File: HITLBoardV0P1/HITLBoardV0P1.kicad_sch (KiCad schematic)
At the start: 0 parts

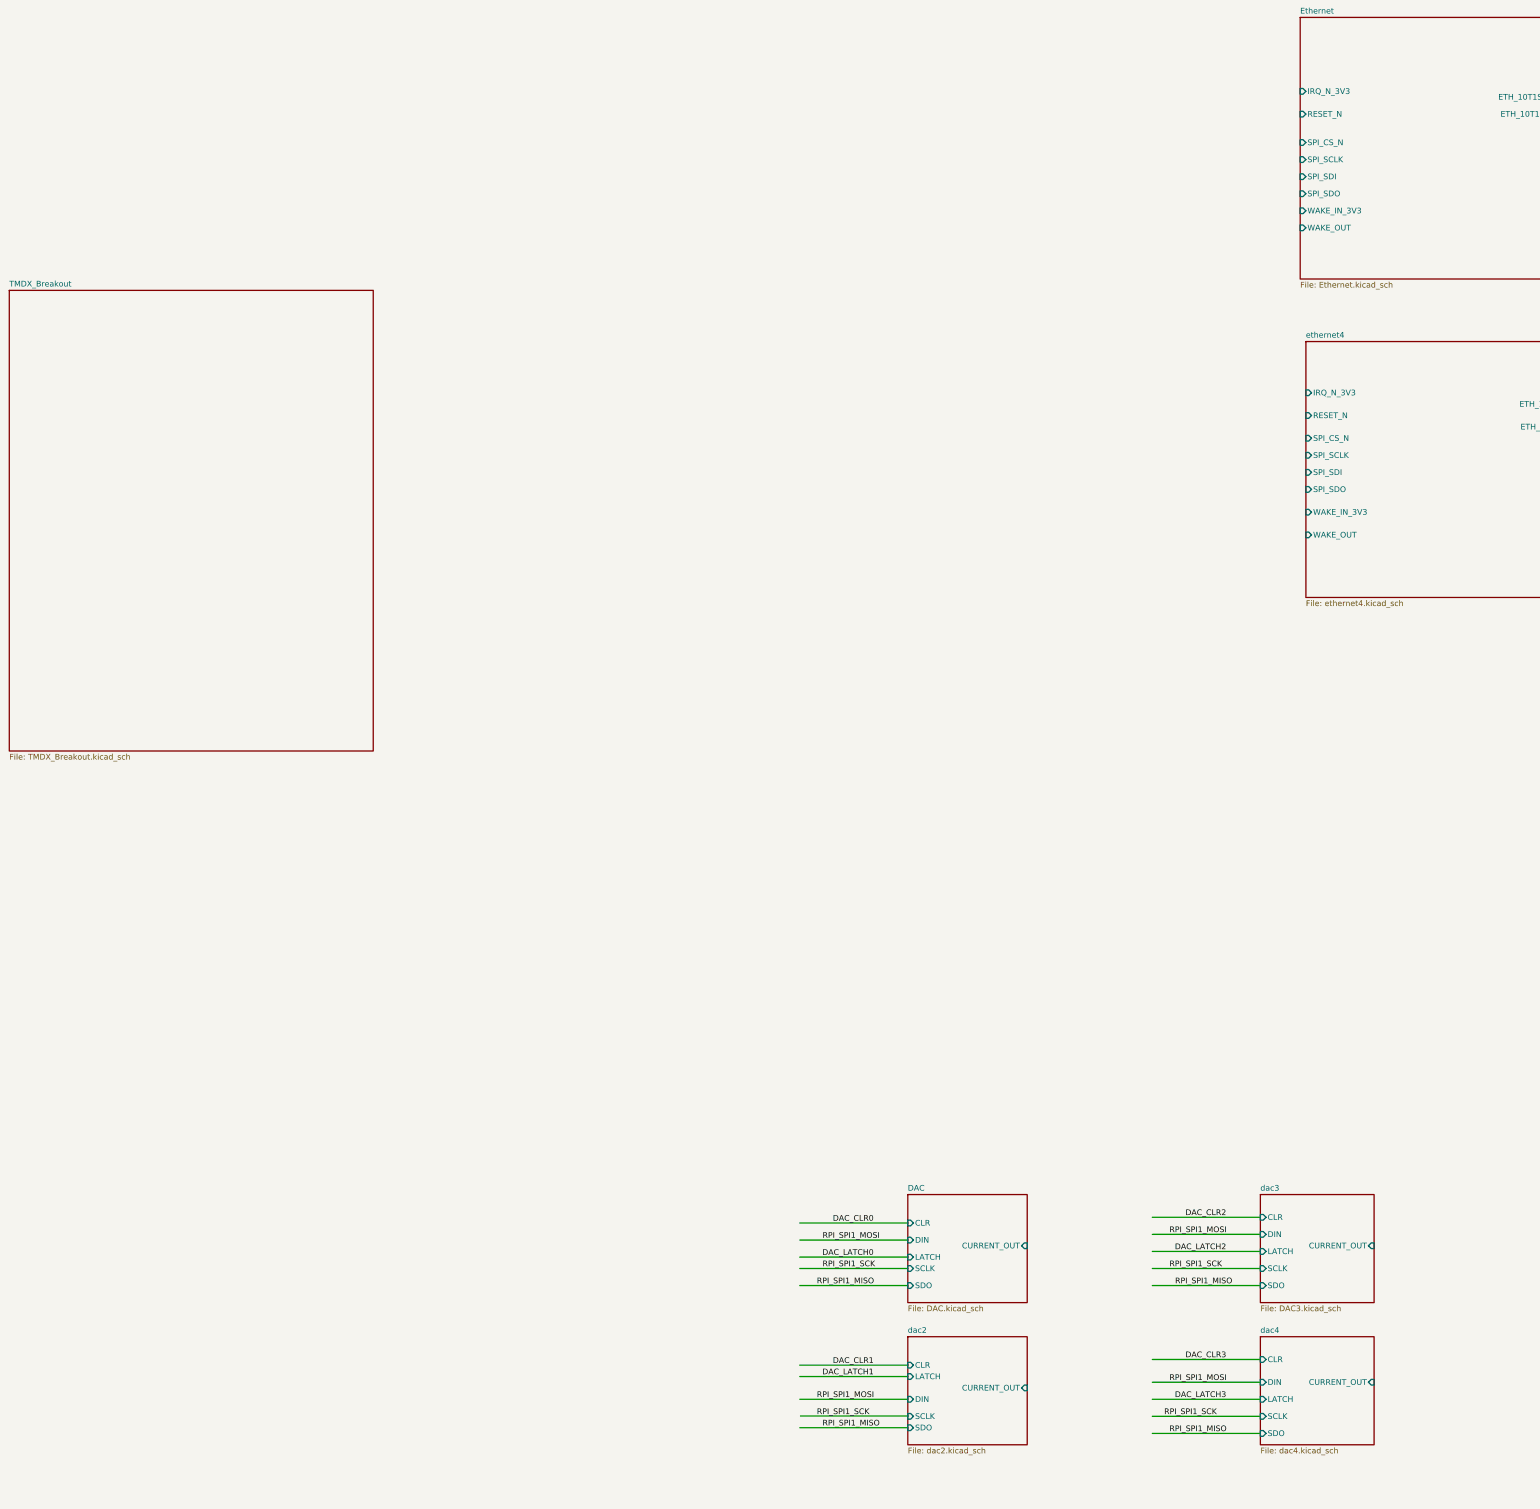
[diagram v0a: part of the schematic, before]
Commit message: update to board with spi buses assigned
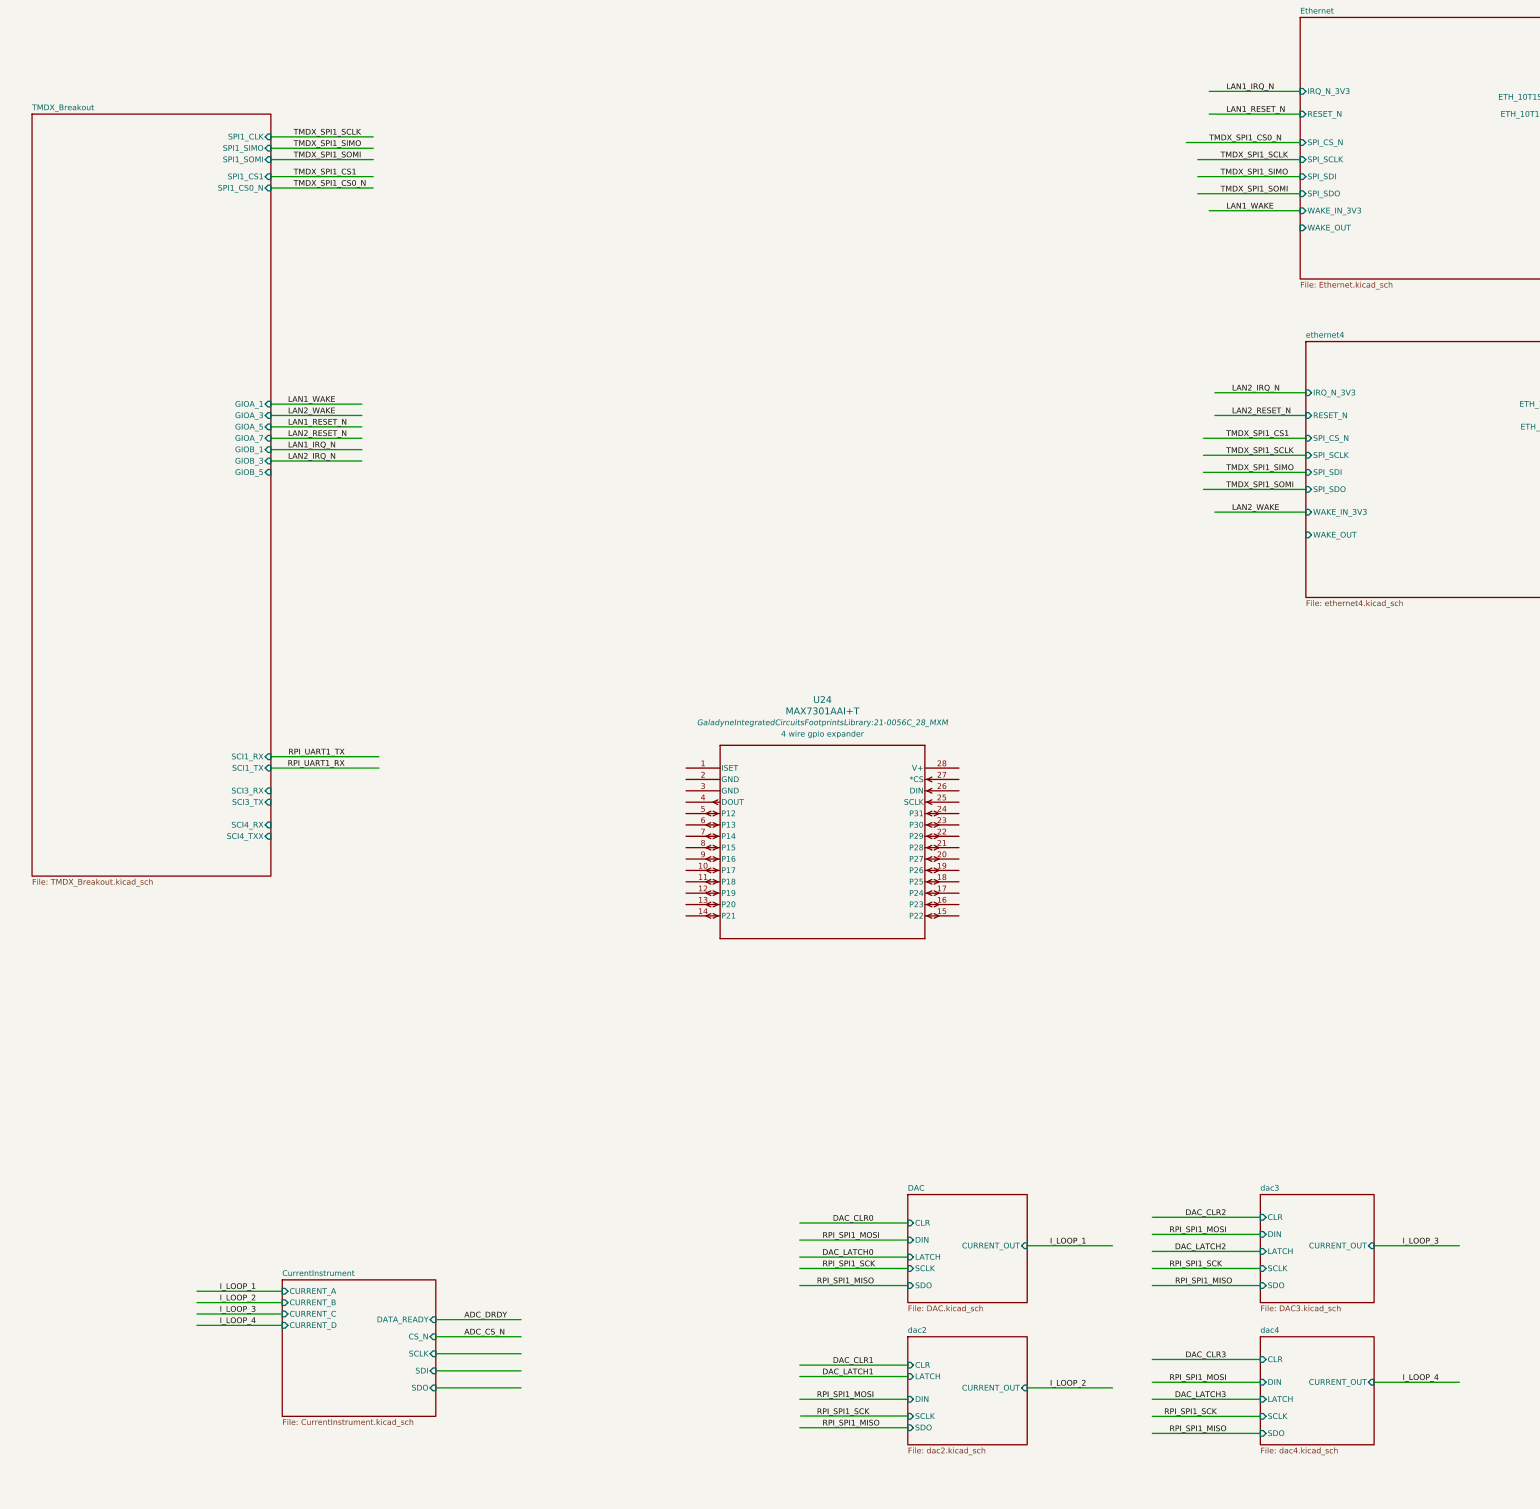
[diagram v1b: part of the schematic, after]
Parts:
- added U24: MAX7301AAI+T, GaladyneIntegratedCircuitsFootprintsLibrary:21-0056C_28_MXM, symbol GaladyneIntegratedCircuitsLibrary:MAX7301AAI+T
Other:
- added sheet CurrentInstrument (CurrentInstrument.kicad_sch)
- sheet TMDX_Breakout ports: added GIOA_1, GIOA_3, GIOA_5, GIOA_7, GIOB_1, GIOB_3, GIOB_5, SCI1_RX, SCI1_TX, SCI3_RX, SCI3_TX, SCI4_RX, SCI4_TXX, SPI1_CLK, SPI1_CS0_N, SPI1_CS1, SPI1_SIMO, SPI1_SOMI; removed none

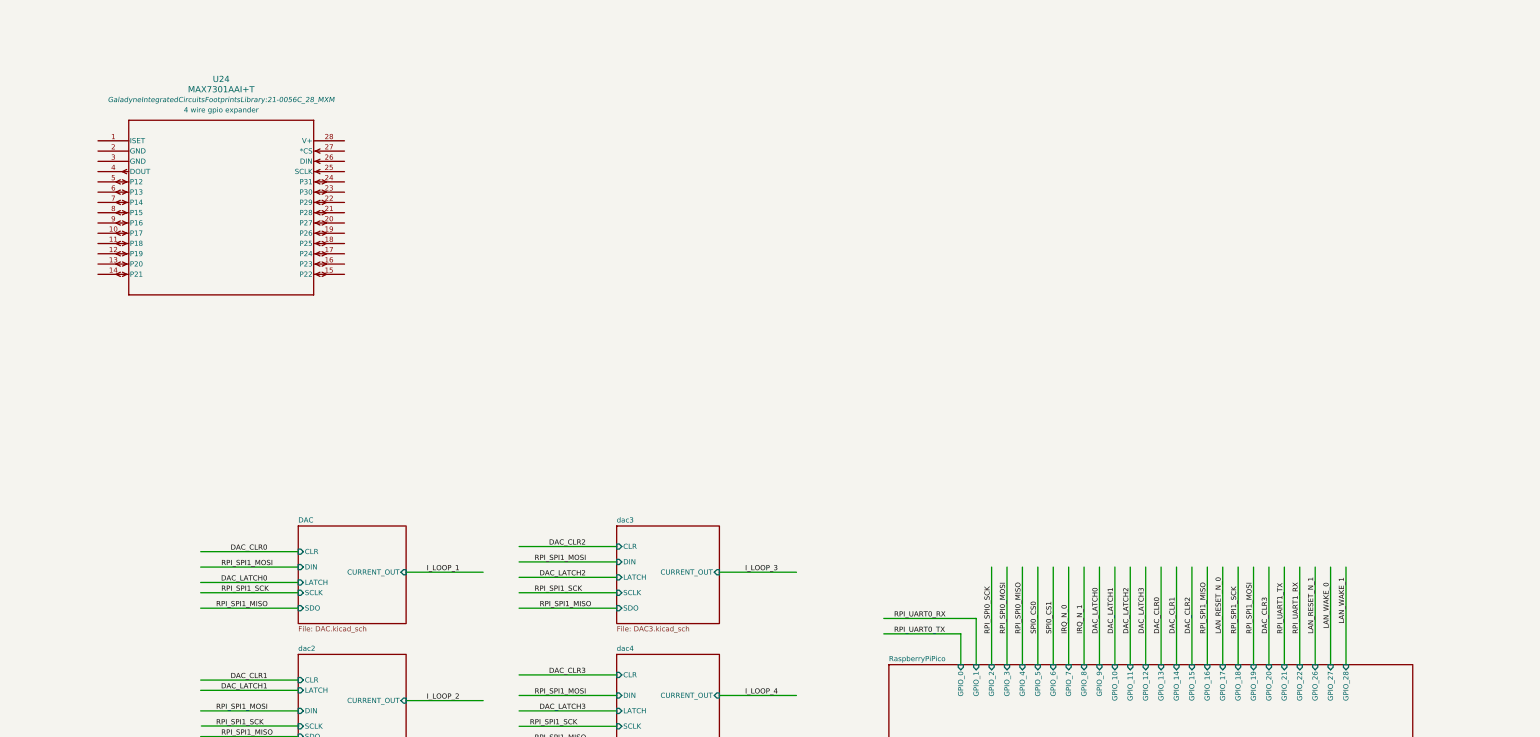
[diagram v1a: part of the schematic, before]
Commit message: ADD GPIO EXPANDER FOR RPI PICO
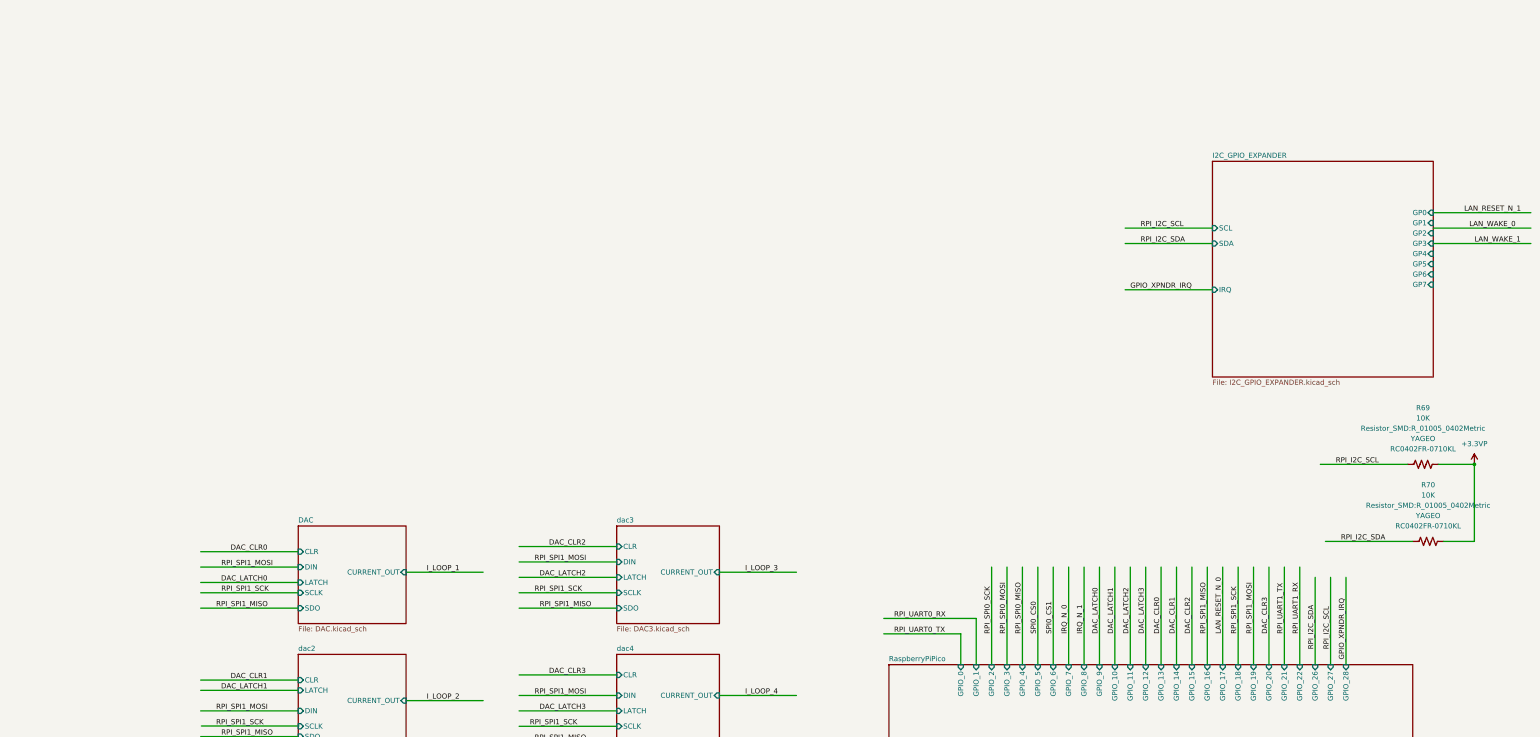
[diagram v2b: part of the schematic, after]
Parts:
- removed U24: MAX7301AAI+T, GaladyneIntegratedCircuitsFootprintsLibrary:21-0056C_28_MXM, symbol GaladyneIntegratedCircuitsLibrary:MAX7301AAI+T
- added R69, R70: 10K, Resistor_SMD:R_01005_0402Metric, symbol Device:R_US
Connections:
- new net +3.3VP: R69.1, R70.1
- new net RPI_I2C_SCL: R69.2
- new net RPI_I2C_SDA: R70.2
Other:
- added sheet I2C_GPIO_EXPANDER (I2C_GPIO_EXPANDER.kicad_sch)
